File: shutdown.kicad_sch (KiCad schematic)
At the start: 19 parts, among them J2 Screw_Terminal_01x02, U6 AP62300TWU, U7 AP62300TWU

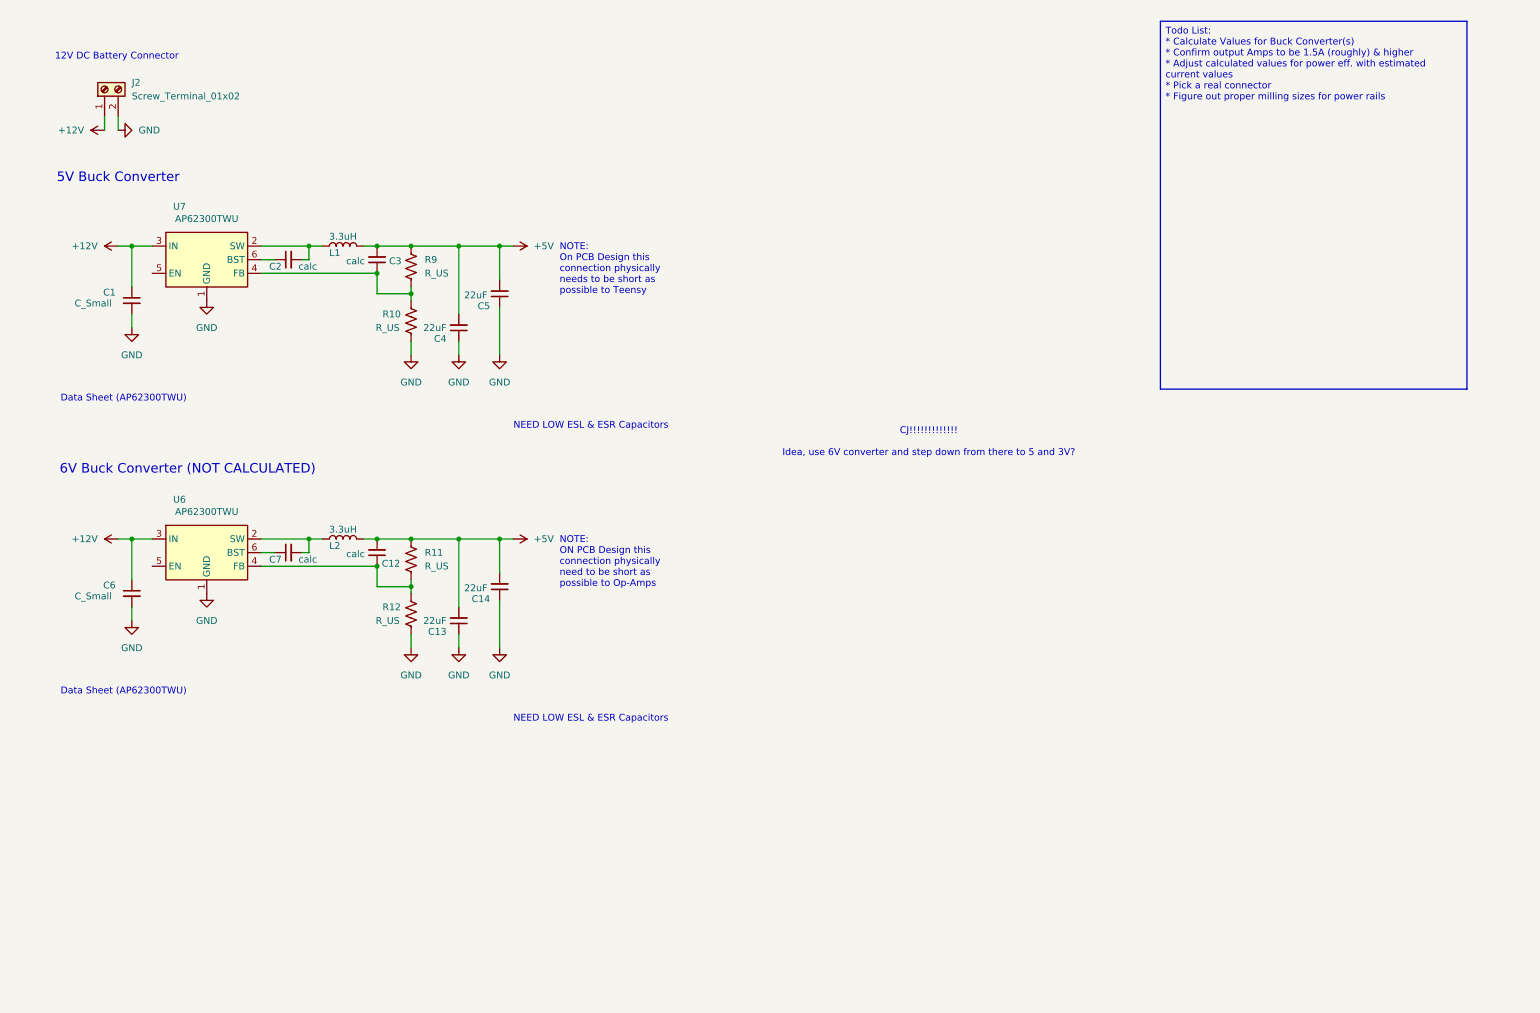
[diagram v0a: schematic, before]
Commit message: Teensy Pins, SDC, Fault Signal Construction
*4 Additional Signal Input Filters
*SDC Completed (need component selection)
*Test points added
*Fault Signal Construction using comparators (more quick, more accurate than voltage divider)
*Considerations: noise - construction of pcb, additional filters; faults - latching, teensy (complete control), fault signals - testing required
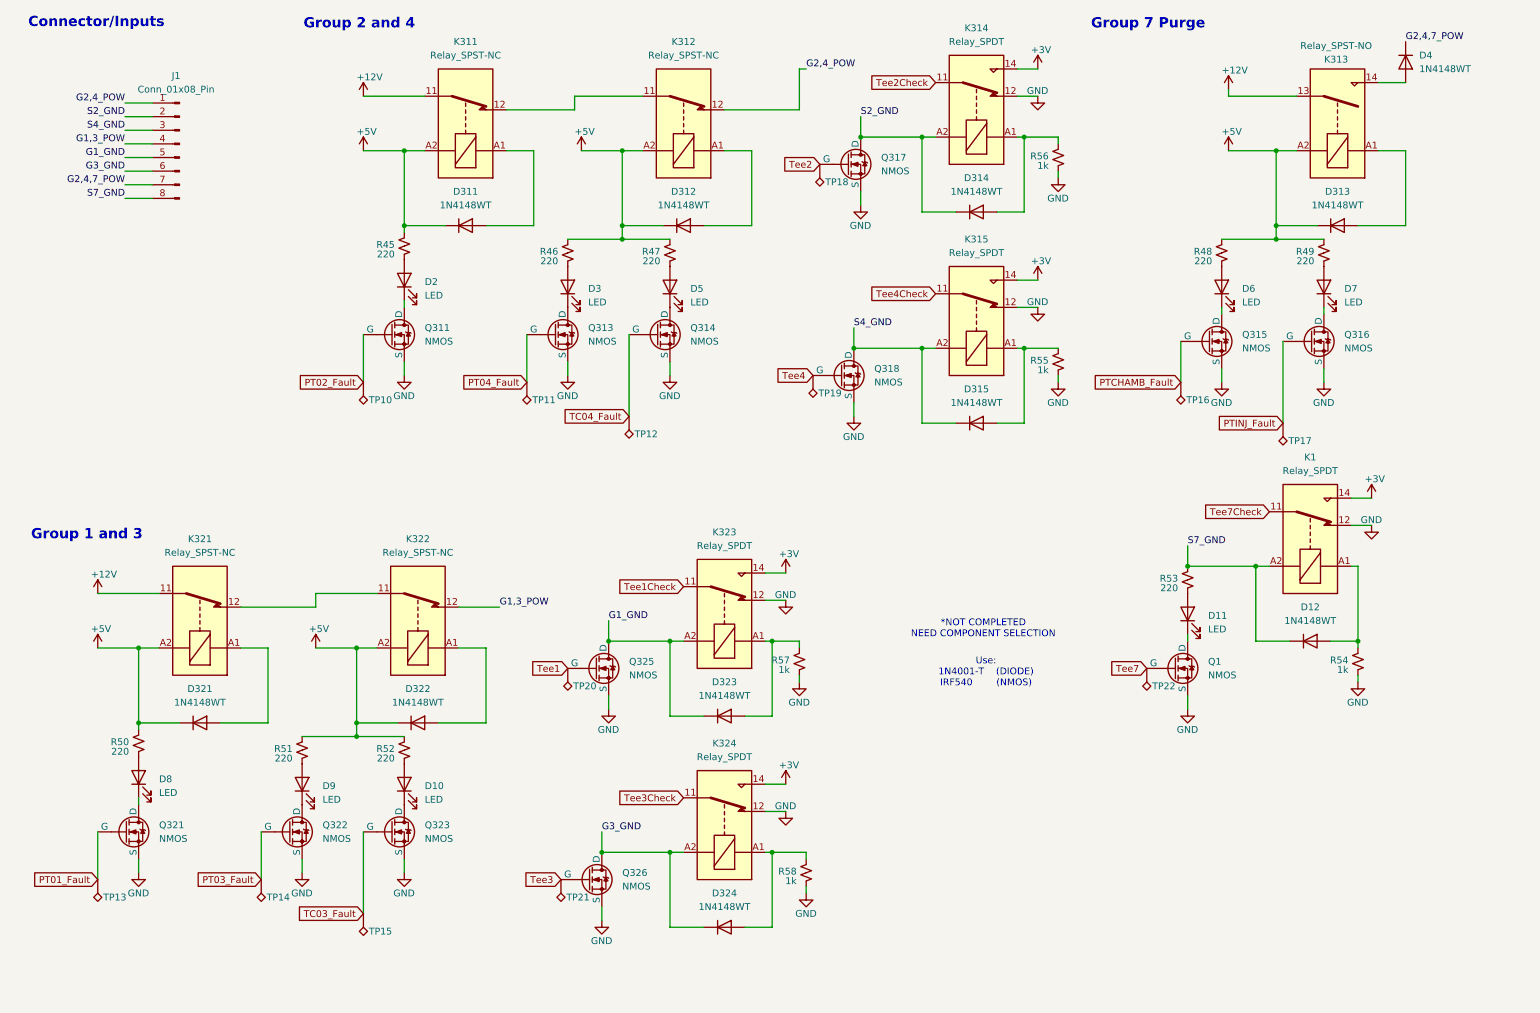
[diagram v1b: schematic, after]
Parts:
- removed C1, C6: C_Small, symbol Device:C_Small
- removed C12, C2, C3, C7: calc, symbol Device:C_Small
- removed C13, C14, C4, C5: 22uF, symbol Device:C_Small
- removed J2: Screw_Terminal_01x02, symbol Connector:Screw_Terminal_01x02
- removed L1, L2: 3.3uH, symbol Device:L
- removed R10, R11, R12, R9: R_US, symbol Device:R_US
- removed U6, U7: AP62300TWU, Package_TO_SOT_SMD:TSOT-23-6, symbol Regulator_Switching:AP62300TWU
- added D10, D11, D2, D3, D5, D6, D7, D8, D9: LED, symbol Device:LED
- added D12, D311, D312, D313, D314, D315, D321, D322, D323, D324, D4: 1N4148WT, Diode_SMD:D_SOD-523, symbol Diode:1N4148WT
- added J1: Conn_01x08_Pin, symbol Connector:Conn_01x08_Pin
- added K1, K314, K315, K323, K324: Relay_SPDT, symbol Relay:Relay_SPDT
- added K311, K312, K321, K322: Relay_SPST-NC, symbol Relay:Relay_SPST-NC
- added K313: Relay_SPST-NO, symbol Relay:Relay_SPST-NO
- added Q1, Q311, Q313, Q314, Q315, Q316, Q317, Q318, Q321, Q322, Q323, Q325, Q326: NMOS, symbol Simulation_SPICE:NMOS
- added R45, R46, R47, R48, R49, R50, R51, R52, R53: 220, symbol Device:R_Small_US
- added R54, R55, R56, R57, R58: 1k, symbol Device:R_Small_US
- added TP10, TP11, TP12, TP13, TP14, TP15, TP16, TP17, TP18, TP19, TP20, TP21, TP22: TestPoint_Alt, symbol Connector:TestPoint_Alt
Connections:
- net +12V: now also K311.11, K313.13, K321.11
- net +5V: now also D311.1 (K), D312.1 (K), D313.1 (K), D321.1 (K), D322.1 (K), K311.A2, K312.A2, K313.A2, K321.A2, K322.A2, R45.1, R46.1, R47.1, R48.1, R49.1, R50.1, R51.1, R52.1
- net GND: now also K1.12, K314.12, K315.12, K323.12, K324.12, Q1.3 (S), Q311.3 (S), Q313.3 (S), Q314.3 (S), Q315.3 (S), Q316.3 (S), Q317.3 (S), Q318.3 (S), Q321.3 (S), Q322.3 (S), Q323.3 (S), Q325.3 (S), Q326.3 (S), R54.2, R55.2, R56.2, R57.2, R58.2
- new net: K311.12, K312.11
- new net: D311.2 (A), K311.A1
- new net: D315.2 (A), K315.A1, R55.1
- new net: D314.2 (A), K314.A1, R56.1
- new net: D11.1 (K), Q1.1 (D)
- new net: D11.2 (A), R53.2
- new net: D9.1 (K), Q322.1 (D)
- new net: D7.1 (K), Q316.1 (D)
- new net: D3.2 (A), R46.2
- new net: D312.2 (A), K312.A1
- new net: K321.12, K322.11
- new net: D321.2 (A), K321.A1
- new net: D322.2 (A), K322.A1
- new net: D8.2 (A), R50.2
- new net: D12.2 (A), K1.A1, R54.1
- new net: D9.2 (A), R51.2
- new net: D324.2 (A), K324.A1, R58.1
- new net: D5.2 (A), R47.2
- new net: D6.2 (A), R48.2
- new net: D2.1 (K), Q311.1 (D)
- new net: D2.2 (A), R45.2
- new net: D3.1 (K), Q313.1 (D)
- new net: D10.1 (K), Q323.1 (D)
- new net: D10.2 (A), R52.2
- new net: D5.1 (K), Q314.1 (D)
- new net: D323.2 (A), K323.A1, R57.1
- new net: D7.2 (A), R49.2
- new net: D4.2 (A), K313.14
- new net: D313.2 (A), K313.A1
- new net: D6.1 (K), Q315.1 (D)
- new net: D8.1 (K), Q321.1 (D)
- new net +3V: K1.14, K314.14, K315.14, K323.14, K324.14
- new net G1,3_POW: J1.4 (Pin_4), K322.12
- new net G1_GND: D323.1 (K), J1.5 (Pin_5), K323.A2, Q325.1 (D)
- new net G2,4,7_POW: D4.1 (K), J1.7 (Pin_7)
- new net G2,4_POW: J1.1 (Pin_1), K312.12
- new net G3_GND: D324.1 (K), J1.6 (Pin_6), K324.A2, Q326.1 (D)
- new net PT01_Fault: Q321.2 (G), TP13.1
- new net PT02_Fault: Q311.2 (G), TP10.1
- new net PT03_Fault: Q322.2 (G), TP14.1
- new net PT04_Fault: Q313.2 (G), TP11.1
- new net PTCHAMB_Fault: Q315.2 (G), TP16.1
- new net PTINJ_Fault: Q316.2 (G), TP17.1
- new net S2_GND: D314.1 (K), J1.2 (Pin_2), K314.A2, Q317.1 (D)
- new net S4_GND: D315.1 (K), J1.3 (Pin_3), K315.A2, Q318.1 (D)
- new net S7_GND: D12.1 (K), J1.8 (Pin_8), K1.A2, R53.1
- new net TC03_Fault: Q323.2 (G), TP15.1
- new net TC04_Fault: Q314.2 (G), TP12.1
- new net Tee1: Q325.2 (G), TP20.1
- new net Tee1Check: K323.11
- new net Tee2: Q317.2 (G), TP18.1
- new net Tee2Check: K314.11
- new net Tee3: Q326.2 (G), TP21.1
- new net Tee3Check: K324.11
- new net Tee4: Q318.2 (G), TP19.1
- new net Tee4Check: K315.11
- new net Tee7: Q1.2 (G), TP22.1
- new net Tee7Check: K1.11
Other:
- note added: "*NOT COMPLETED NEED COMPONENT SELECTION"
- note added: "Connector/Inputs"
- note added: "Group 1 and 3"
- note added: "Group 2 and 4"
- note added: "Group 7 Purge"
- note added: "Use: 1N4001-T (DIODE) IRF540 (NMOS)"
- note removed: "12V DC Battery Connector"
- note removed: "5V Buck Converter"
- note removed: "6V Buck Converter (NOT CALCULATED)"
- note removed: "CJ!!!!!!!!!!!!! Idea, use 6V converter and step down from there to 5 and 3V?"
- note removed: "Data Sheet (AP62300TWU)"
- note removed: "NEED LOW ESL & ESR Capacitors"
- note removed: "NOTE: ON PCB Design this connection physically need to be short as possible to Op-Amps"
- note removed: "NOTE: On PCB Design this connection physically needs to be short as possible to Teensy"
- title: Power Supply -> (none)

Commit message: Voltage Fix, Tri-State Buffers, Double-Buffer
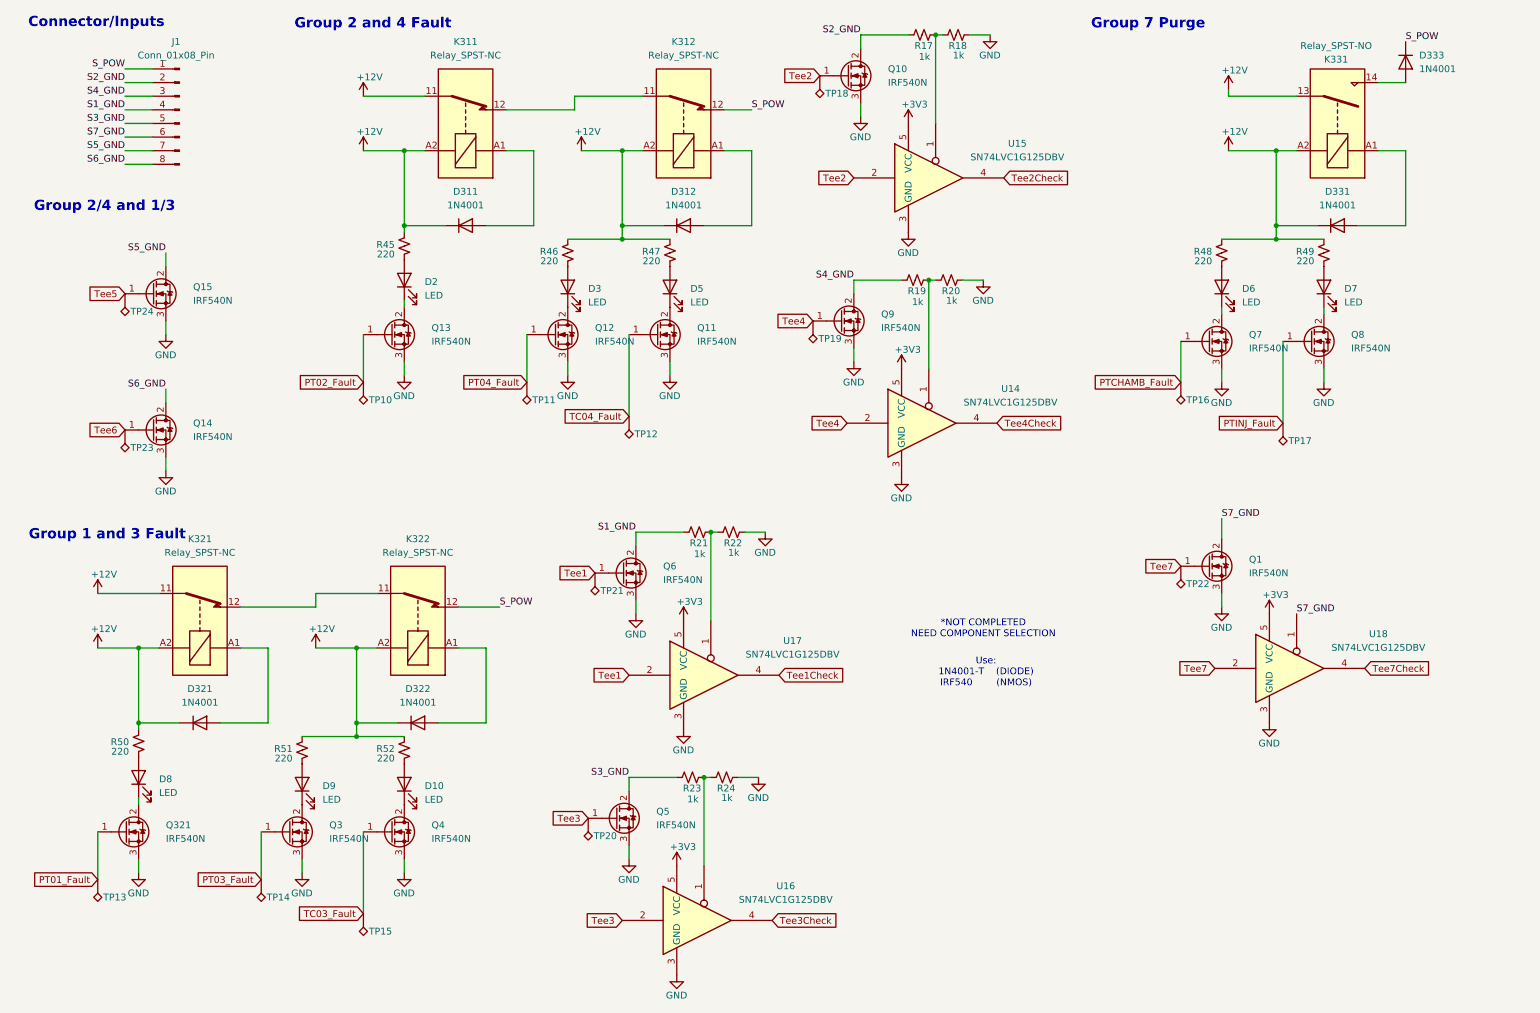
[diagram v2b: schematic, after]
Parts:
- removed D11: LED, symbol Device:LED
- removed D12, D311, D312, D313, D314, D315, D321, D322, D323, D324, D4: 1N4148WT, Diode_SMD:D_SOD-523, symbol Diode:1N4148WT
- removed K1, K314, K315, K323, K324: Relay_SPDT, symbol Relay:Relay_SPDT
- removed Q1, Q311, Q313, Q314, Q315, Q316, Q317, Q318, Q321, Q322, Q323, Q325, Q326: NMOS, symbol Simulation_SPICE:NMOS
- removed R53: 220, symbol Device:R_Small_US
- removed R54, R55, R56, R57, R58: 1k, symbol Device:R_Small_US
- added D311, D312, D321, D322, D331, D333: 1N4001, Diode_THT:D_DO-41_SOD81_P10.16mm_Horizontal, symbol Diode:1N4001
- added Q1, Q10, Q11, Q12, Q13, Q14, Q15, Q3, Q321, Q4, Q5, Q6, Q7, Q8, Q9: IRF540N, Package_TO_SOT_THT:TO-220-3_Vertical, symbol Transistor_FET:IRF540N
- added R17, R18, R19, R20, R21, R22, R23, R24: 1k, symbol Device:R_Small_US
- added TP23, TP24: TestPoint_Alt, symbol Connector:TestPoint_Alt
- added U14, U15, U16, U17, U18: SN74LVC1G125DBV, Package_TO_SOT_SMD:SOT-23-5, symbol 74xGxx:SN74LVC1G125DBV
- renumbered K313 to K331
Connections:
- net +5V is gone; now on net +12V: K311.A2, K312.A2, K321.A2, K322.A2, K331.A2, R45.1, R46.1, R47.1, R48.1, R49.1, R50.1, R51.1, R52.1
- net G3_GND is gone; now on net S7_GND: J1.6 (Pin_6)
- net +12V: now also D311.1 (K), D312.1 (K), D321.1 (K), D322.1 (K), D331.1 (K)
- net GND: now also Q1.3 (S), Q10.3 (S), Q11.3 (S), Q12.3 (S), Q13.3 (S), Q14.3 (S), Q15.3 (S), Q3.3 (S), Q321.3 (S), Q4.3 (S), Q5.3 (S), Q6.3 (S), Q7.3 (S), Q8.3 (S), Q9.3 (S), R18.2, R20.2, R22.2, R24.2, U14.3 (GND), U15.3 (GND), U16.3 (GND), U17.3 (GND), U18.3 (GND)
- net PT01_Fault: now also Q321.1 (G)
- net PT02_Fault: now also Q13.1 (G)
- net PT03_Fault: now also Q3.1 (G)
- net PT04_Fault: now also Q12.1 (G)
- net PTCHAMB_Fault: now also Q7.1 (G)
- net PTINJ_Fault: now also Q8.1 (G)
- net S2_GND: now also Q10.2 (D), R17.1
- net S4_GND: now also Q9.2 (D), R19.1
- net S7_GND: now also Q1.2 (D), U18.1; no longer J1.8 (Pin_8)
- net TC03_Fault: now also Q4.1 (G)
- net TC04_Fault: now also Q11.1 (G)
- net Tee1: now also TP21.1, Q6.1 (G), U17.2; no longer TP20.1
- net Tee1Check: now also U17.4
- net Tee2: now also Q10.1 (G), U15.2
- net Tee2Check: now also U15.4
- net Tee3: now also TP20.1, Q5.1 (G), U16.2; no longer TP21.1
- net Tee3Check: now also U16.4
- net Tee4: now also Q9.1 (G), U14.2
- net Tee4Check: now also U14.4
- net Tee7: now also Q1.1 (G), U18.2
- net Tee7Check: now also U18.4
- net at K311.A1: now also D311.2 (A)
- net at D9.1 (K): now also Q3.2 (D)
- net at D7.1 (K): now also Q8.2 (D)
- net at K312.A1: now also D312.2 (A)
- net at K321.A1: now also D321.2 (A)
- net at K322.A1: now also D322.2 (A)
- net at D2.1 (K): now also Q13.2 (D)
- net at D3.1 (K): now also Q12.2 (D)
- net at D10.1 (K): now also Q4.2 (D)
- net at D5.1 (K): now also Q11.2 (D)
- net at K331.14: now also D333.2 (A)
- net at K331.A1: now also D331.2 (A)
- net at D6.1 (K): now also Q7.2 (D)
- net at D8.1 (K): now also Q321.2 (D)
- net G1,3_POW renamed S1_GND
- net S1_GND: now also Q6.2 (D), R21.1; no longer K322.12
- net G1_GND renamed S3_GND
- net S3_GND: now also Q5.2 (D), R23.1
- net G2,4,7_POW renamed S5_GND
- net S5_GND: now also Q15.2 (D)
- net G2,4_POW renamed S_POW
- net S_POW: now also K322.12, D333.1 (K)
- new net: R21.2, R22.1, U17.1
- new net: R23.2, R24.1, U16.1
- new net: R19.2, R20.1, U14.1
- new net: R17.2, R18.1, U15.1
- new net +3V3: U14.5 (VCC), U15.5 (VCC), U16.5 (VCC), U17.5 (VCC), U18.5 (VCC)
- new net S6_GND: J1.8 (Pin_8), Q14.2 (D)
- new net Tee5: Q15.1 (G), TP24.1
- new net Tee6: Q14.1 (G), TP23.1
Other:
- note added: "Group 1 and 3 Fault"
- note added: "Group 2 and 4 Fault"
- note added: "Group 2/4 and 1/3"
- note removed: "Group 1 and 3"
- note removed: "Group 2 and 4"
- moved on the sheet: J1, TP19
